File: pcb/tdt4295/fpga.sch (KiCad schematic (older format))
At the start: 39 parts, among them J1 FPGA__debug

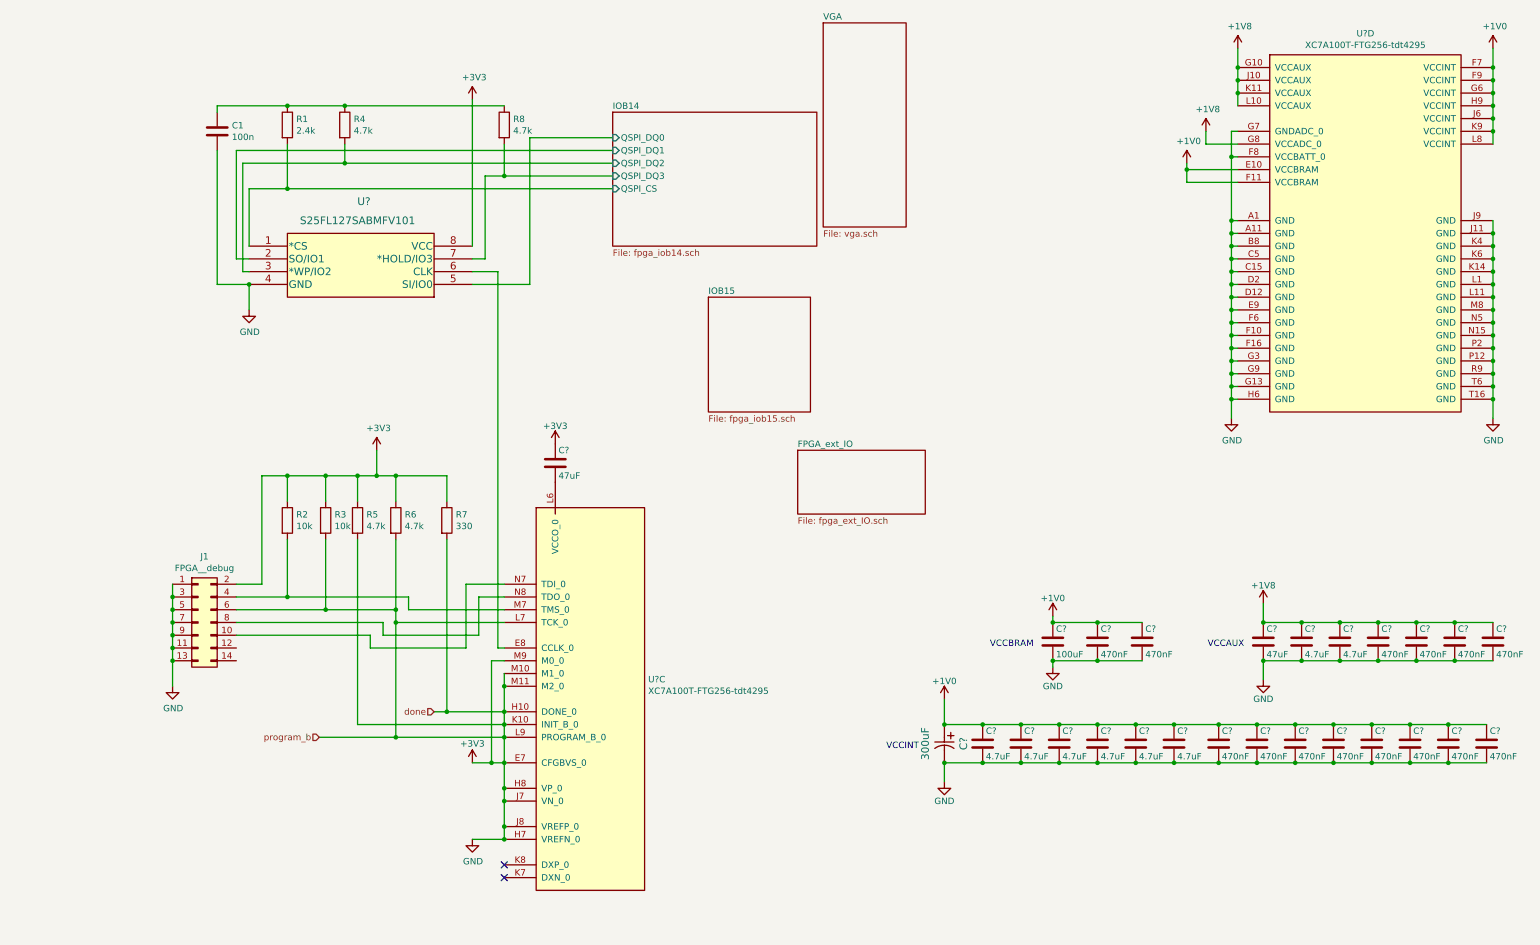
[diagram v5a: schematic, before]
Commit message: associate symbol components
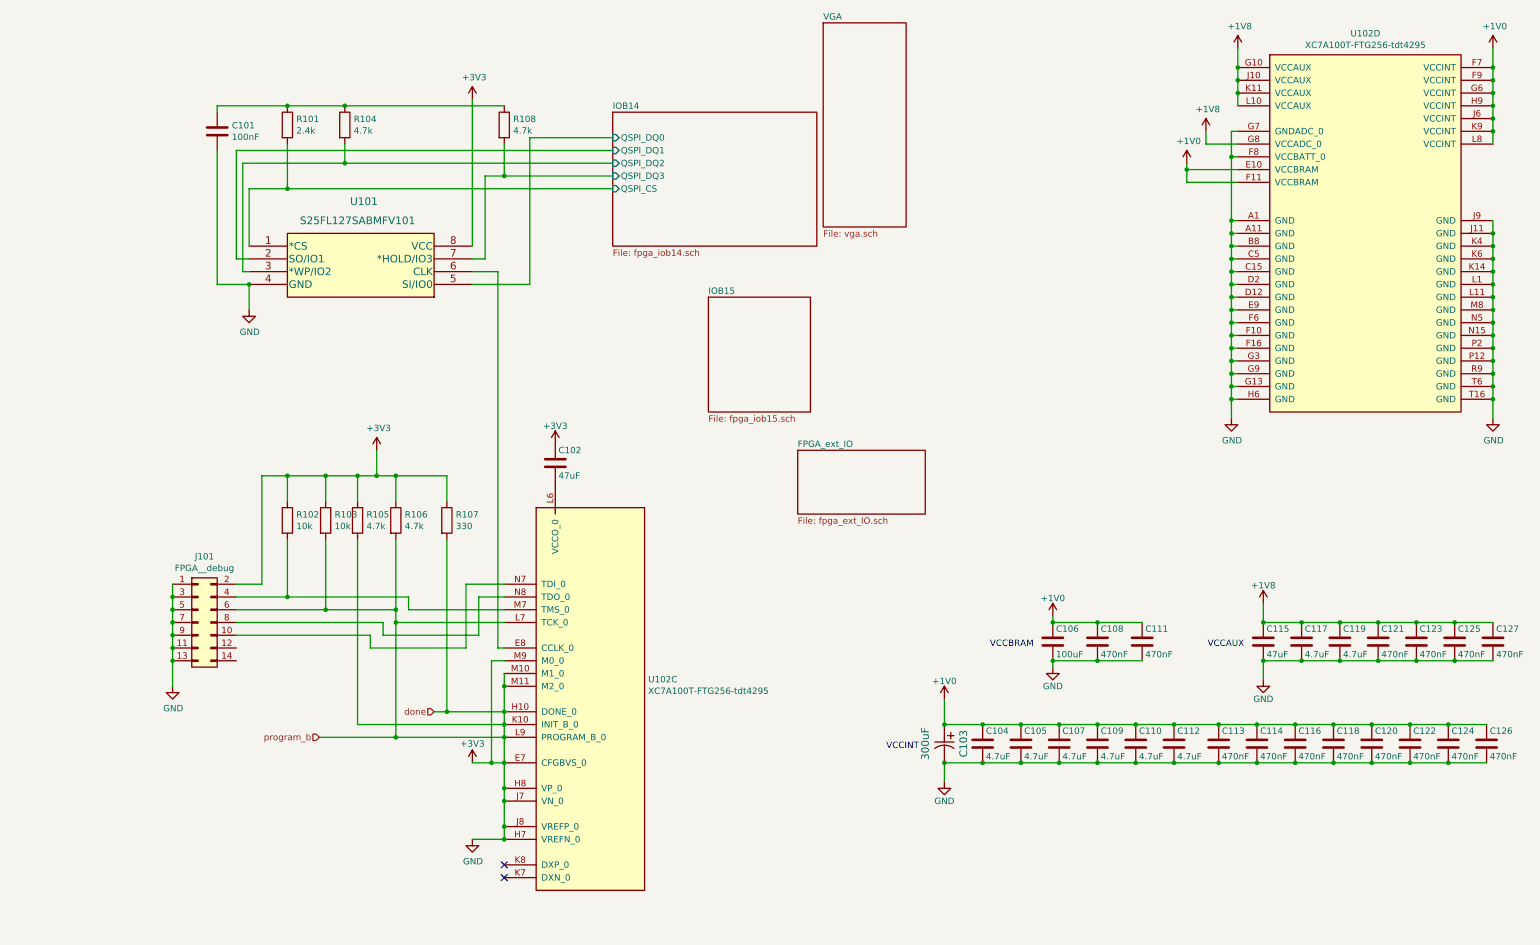
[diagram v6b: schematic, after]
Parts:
- C101: renamed from C1; value 100n -> 100nF
- U101: renamed from U?; footprint SOC008_SPA -> S25FL127SABMFV101-footprint:S25FL127SABMFV101
- U102: renamed from U?; footprint (none) -> Package_BGA:Xilinx_FTG256
- gave numbers to parts that had none: 26
- renumbered J1 to J101, R1 to R101, R2 to R102, R3 to R103, R4 to R104, R5 to R105, R6 to R106, R7 to R107, R8 to R108

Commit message: Major restructuring of FPGA outputs
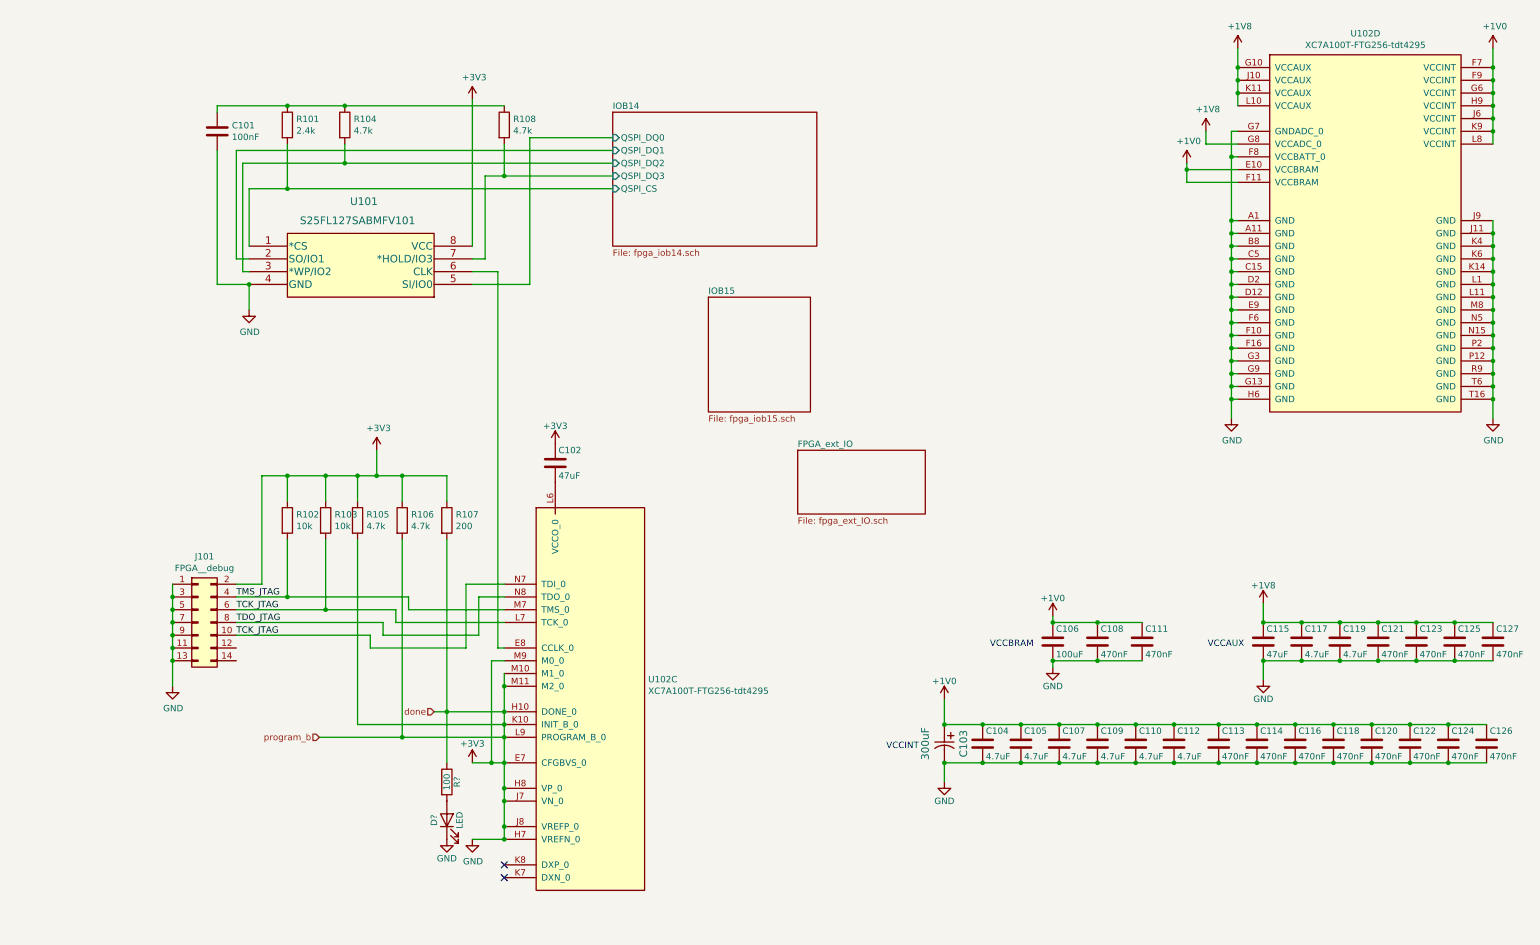
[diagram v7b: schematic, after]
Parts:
- added D?: LED, symbol Device:LED
- added R?: 100, symbol Device:R
- R107: value 330 -> 200
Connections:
- net +3V3: now also D?.1 (K), R?.1; no longer J101.6 (Pin_6), R103.2, U102.L7 (TCK_0)
- net TMS_JTAG: now reaches J101.4 (Pin_4), R102.2, U102.M7 (TMS_0)
- net TCK_JTAG: now reaches J101.10 (Pin_10), U102.N7 (TDI_0)
- net TCK_JTAG: now also J101.6 (Pin_6), R103.2, U102.L7 (TCK_0)
- net TDO_JTAG: now reaches J101.8 (Pin_8), U102.N8 (TDO_0)
- new net: D?.2 (A), R?.2
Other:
- moved on the sheet: R106

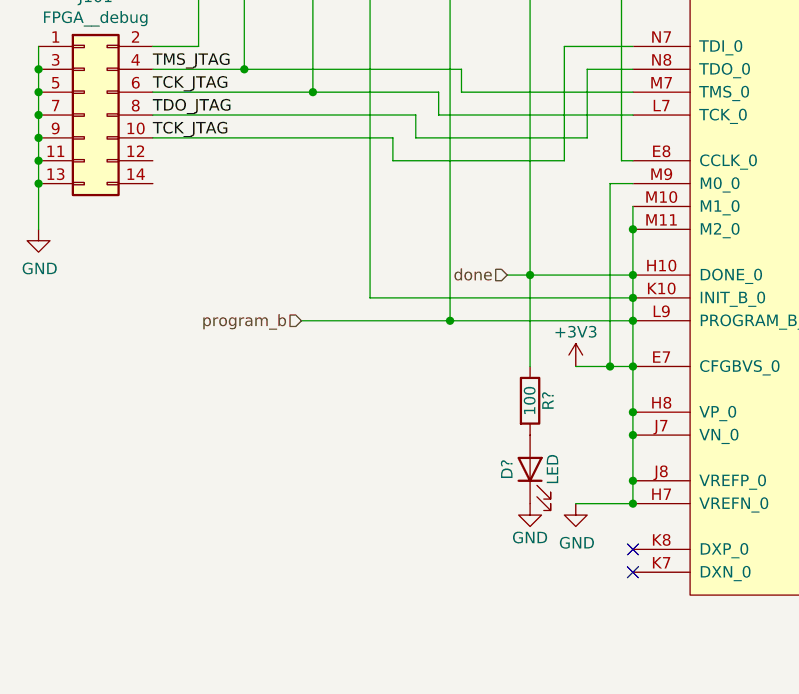
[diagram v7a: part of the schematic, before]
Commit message: add configuration modes
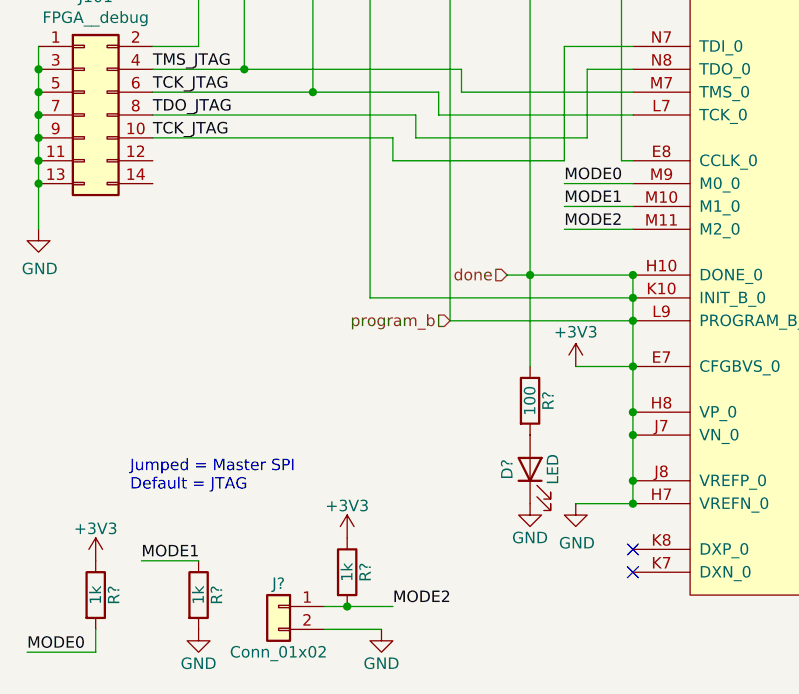
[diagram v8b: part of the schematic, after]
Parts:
- added J?: Conn_01x02, symbol Connector_Generic:Conn_01x02
- added R? (x3): 1k, symbol Device:R
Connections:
- net +3V3: now also J?.2 (Pin_2), R?.1, R?.1, R?.2; no longer U102.M10 (M1_0), U102.M11 (M2_0), U102.M9 (M0_0)
- new net MODE0: R?.2, U102.M9 (M0_0)
- new net MODE1: R?.1, U102.M10 (M1_0)
- new net MODE2: J?.1 (Pin_1), R?.2, U102.M11 (M2_0)
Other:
- note added: "Jumped = Master SPI\nDefault = JTAG"
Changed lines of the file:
@@
 Wire Wire Line
 	2350 6200 3150 6200
-Connection ~ 2350 6200
 Wire Wire Line
 	2150 4150 2350 4150
@@
 	2350 4150 2700 4150
 Connection ~ 2350 4150
-Wire Wire Line
-	1700 6200 2350 6200
 Wire Wire Line
 	2350 4650 2350 6200
@@
 Connection ~ 3150 6000
 Wire Wire Line
-	3150 5800 3150 6000
-Connection ~ 3150 5800
-Wire Wire Line
-	3150 5700 3150 5800
-$Comp
-L power:+3V3 #PWR0105
-U 1 1 6176AD1A
-P 2900 6400
-F 0 "#PWR0105" H 2900 6250 50  0001 C CNN
-F 1 "+3V3" H 2900 6550 50  0000 C CNN
-F 2 "" H 2900 6400 50  0001 C CNN
-F 3 "" H 2900 6400 50  0001 C CNN
-	1    2900 6400
-	1    0    0    -1
-$EndComp
-Wire Wire Line
-	3050 6400 3150 6400
-Connection ~ 3050 6400
-Wire Wire Line
-	2900 6400 3050 6400
-Wire Wire Line
-	3050 5600 3050 6400
-Wire Wire Line
-	3150 5600 3050 5600
-Wire Wire Line
 	1150 1900 1450 1900
 Wire Wire Line
@@
 	-1   0    0    -1
 $EndComp
-Text HLabel 1700 6200 0    50   Input ~ 0
+Text HLabel 2350 6200 0    50   Input ~ 0
 program_b
 NoConn ~ 3150 7300
@@
 Text Label 1050 5400 0    50   ~ 0
 TCK_JTAG
+$Comp
+L power:+3V3 #PWR0105
+U 1 1 6176AD1A
+P 2900 6400
+F 0 "#PWR0105" H 2900 6250 50  0001 C CNN
+F 1 "+3V3" H 2900 6550 50  0000 C CNN
+F 2 "" H 2900 6400 50  0001 C CNN
+F 3 "" H 2900 6400 50  0001 C CNN
+	1    2900 6400
+	1    0    0    -1
+$EndComp
+$Comp
+L Connector_Generic:Conn_01x02 J?
+U 1 1 61879505
+P 1600 7450
+F 0 "J?" H 1600 7550 50  0000 C CNN
+F 1 "Conn_01x02" H 1600 7250 50  0000 C CNN
+F 2 "" H 1600 7450 50  0001 C CNN
+F 3 "~" H 1600 7450 50  0001 C CNN
+	1    1600 7450
+	-1   0    0    -1
+$EndComp
+Wire Wire Line
+	1800 7550 2050 7550
+Text Label 2100 7450 0    50   ~ 0
+MODE2
+Wire Wire Line
+	2900 6400 3150 6400
+Wire Wire Line
+	3150 5600 2850 5600
+Wire Wire Line
+	3150 5700 2850 5700
+Wire Wire Line
+	3150 5800 2850 5800
+Text Label 2850 5600 0    50   ~ 0
+MODE0
+Text Label 2850 5700 0    50   ~ 0
+MODE1
+Text Label 2850 5800 0    50   ~ 0
+MODE2
+$Comp
+L power:GND #PWR?
+U 1 1 618E8B3B
+P 2050 7550
+F 0 "#PWR?" H 2050 7300 50  0001 C CNN
+F 1 "GND" H 2050 7400 50  0000 C CNN
+F 2 "" H 2050 7550 50  0001 C CNN
+F 3 "" H 2050 7550 50  0001 C CNN
+	1    2050 7550
+	1    0    0    -1
+$EndComp
+$Comp
+L Device:R R?
+U 1 1 618E96EF
+P 1900 7300
+F 0 "R?" V 1980 7300 50  0000 C CNN
+F 1 "1k" V 1900 7300 50  0000 C CNN
+F 2 "" V 1830 7300 50  0001 C CNN
+F 3 "~" H 1900 7300 50  0001 C CNN
+	1    1900 7300
+	1    0    0    -1
+$EndComp
+$Comp
+L power:+3V3 #PWR?
+U 1 1 618EA756
+P 1900 7150
+F 0 "#PWR?" H 1900 7000 50  0001 C CNN
+F 1 "+3V3" H 1900 7290 50  0000 C CNN
+F 2 "" H 1900 7150 50  0001 C CNN
+F 3 "" H 1900 7150 50  0001 C CNN
+	1    1900 7150
+	1    0    0    -1
+$EndComp
+Wire Wire Line
+	1800 7450 1900 7450
+Wire Wire Line
+	1900 7450 2100 7450
+Connection ~ 1900 7450
+$Comp
+L Device:R R?
+U 1 1 619371E0
+P 1250 7400
+F 0 "R?" V 1330 7400 50  0000 C CNN
+F 1 "1k" V 1250 7400 50  0000 C CNN
+F 2 "" V 1180 7400 50  0001 C CNN
+F 3 "~" H 1250 7400 50  0001 C CNN
+	1    1250 7400
+	1    0    0    -1
+$EndComp
+$Comp
+L Device:R R?
+U 1 1 61937C9D
+P 800 7400
+F 0 "R?" V 880 7400 50  0000 C CNN
+F 1 "1k" V 800 7400 50  0000 C CNN
+F 2 "" V 730 7400 50  0001 C CNN
+F 3 "~" H 800 7400 50  0001 C CNN
+	1    800  7400
+	1    0    0    -1
+$EndComp
+Wire Wire Line
+	1250 7250 1000 7250
+$Comp
+L power:GND #PWR?
+U 1 1 6195618C
+P 1250 7550
+F 0 "#PWR?" H 1250 7300 50  0001 C CNN
+F 1 "GND" H 1250 7400 50  0000 C CNN
+F 2 "" H 1250 7550 50  0001 C CNN
+F 3 "" H 1250 7550 50  0001 C CNN
+	1    1250 7550
+	1    0    0    -1
+$EndComp
+Text Label 1000 7250 0    50   ~ 0
+MODE1
+Text Label 500  7650 0    50   ~ 0
+MODE0
+$Comp
+L power:+3V3 #PWR?
+U 1 1 619680CF
+P 800 7250
+F 0 "#PWR?" H 800 7100 50  0001 C CNN
+F 1 "+3V3" H 800 7390 50  0000 C CNN
+F 2 "" H 800 7250 50  0001 C CNN
+F 3 "" H 800 7250 50  0001 C CNN
+	1    800  7250
+	1    0    0    -1
+$EndComp
+Wire Wire Line
+	800  7650 800  7550
+Wire Wire Line
+	500  7650 800  7650
+Text Notes 950  6950 0    50   ~ 0
+Jumped = Master SPI\nDefault = JTAG
 $EndSCHEMATC
